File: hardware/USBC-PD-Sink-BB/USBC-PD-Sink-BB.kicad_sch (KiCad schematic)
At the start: 0 parts

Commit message: Started schematic.  Added docs for MCP22031 Sink Board
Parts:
- added J1: USB_C_Receptacle_USB2.0_16P, symbol Connector:USB_C_Receptacle_USB2.0_16P
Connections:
- new net: J1.A1 (GND), J1.A12 (GND), J1.B1 (GND), J1.B12 (GND)
- new net: J1.A4 (VBUS), J1.A9 (VBUS), J1.B4 (VBUS), J1.B9 (VBUS)
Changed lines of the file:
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@@
 		(title "USB C PD Sink Breakout Board")
+	)
+	(symbol
+		(lib_id "Connector:USB_C_Receptacle_USB2.0_16P")
+		(at 31.75 86.36 0)
+		(unit 1)
+		(exclude_from_sim no)
+		(in_bom yes)
+		(on_board yes)
+		(dnp no)
+		(fields_autoplaced yes)
+		(property "Reference" "J1"
+			(at 31.75 63.5 0)
+			(effects
+				(font
+					(size 1.27 1.27)
+				)
+			)
+		)
+		(property "Value" "USB_C_Receptacle_USB2.0_16P"
+			(at 31.75 66.04 0)
+			(effects
+				(font
+					(size 1.27 1.27)
+				)
+			)
+		)
+		(property "Footprint" ""
+			(at 35.56 86.36 0)
+			(effects
+				(font
+					(size 1.27 1.27)
+				)
+				(hide yes)
+			)
+		)
+		(property "Datasheet" "https://www.usb.org/sites/default/files/documents/usb_type-c.zip"
+			(at 35.56 86.36 0)
+			(effects
+				(font
+					(size 1.27 1.27)
+				)
+				(hide yes)
+			)
+		)
+		(property "Description" "USB 2.0-only 16P Type-C Receptacle connector"
+			(at 31.75 86.36 0)
+			(effects
+				(font
+					(size 1.27 1.27)
+				)
+				(hide yes)
+			)
+		)
+		(pin "B6"
+		)
+		(pin "A6"
+		)
+		(pin "B8"
+		)
+		(pin "A8"
+		)
+		(pin "B4"
+		)
+		(pin "B7"
+		)
+		(pin "A12"
+		)
+		(pin "A5"
+		)
+		(pin "A1"
+		)
+		(pin "S1"
+		)
+		(pin "A4"
+		)
+		(pin "A9"
+		)
+		(pin "B9"
+		)
+		(pin "B12"
+		)
+		(pin "B1"
+		)
+		(pin "A7"
+		)
+		(pin "B5"
+		)
+		(instances
+			(project ""
+				(path "/244fbf81-301d-43a9-8691-1c7dc9ccb063"
+					(reference "J1")
+					(unit 1)
+				)
+			)
+		)
 	)
 	(sheet_instances

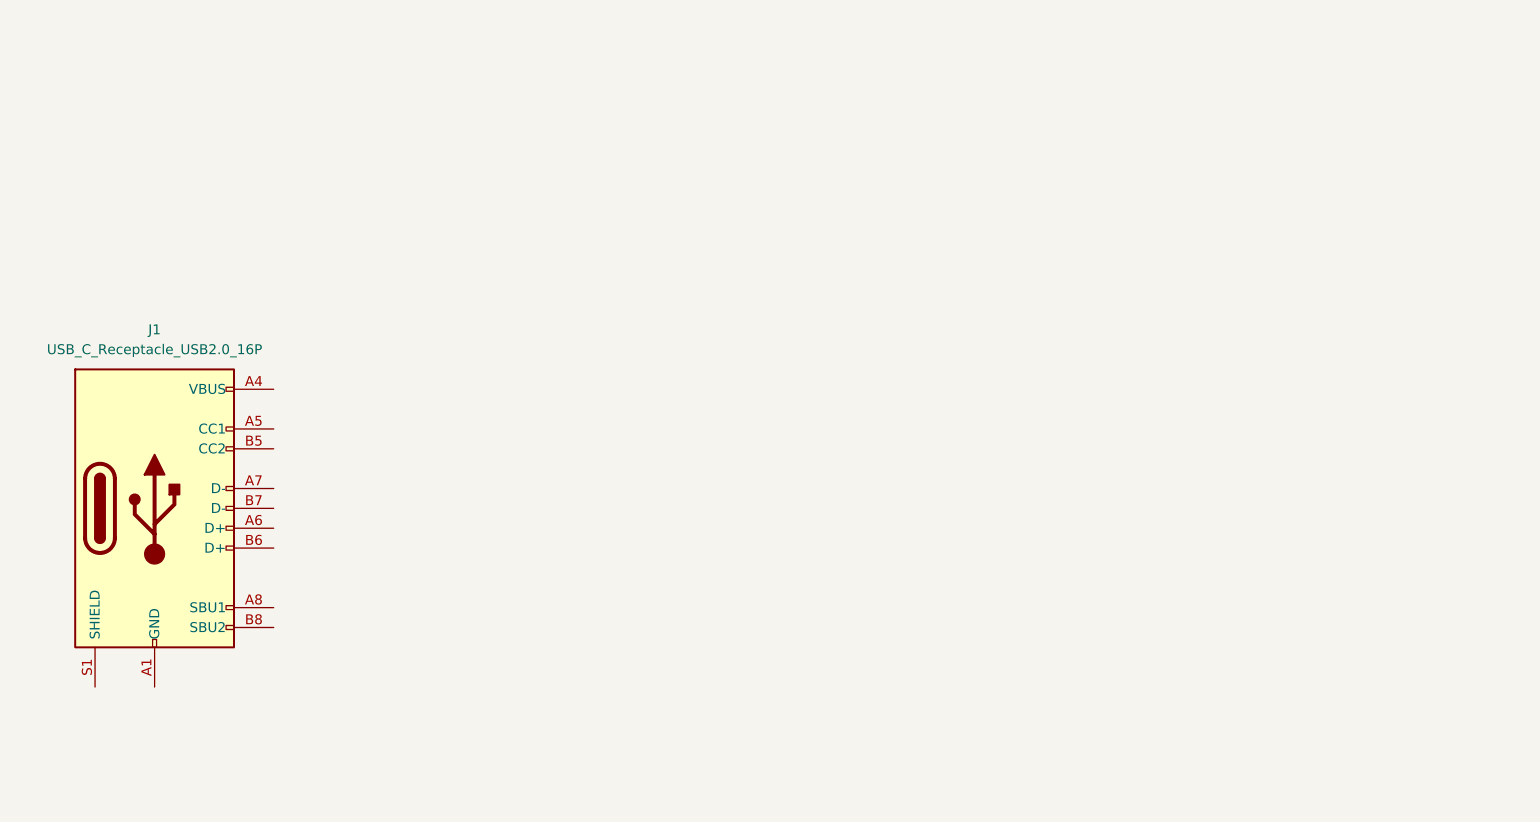
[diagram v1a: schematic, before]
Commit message: Updated schematic.  Added MCP22301
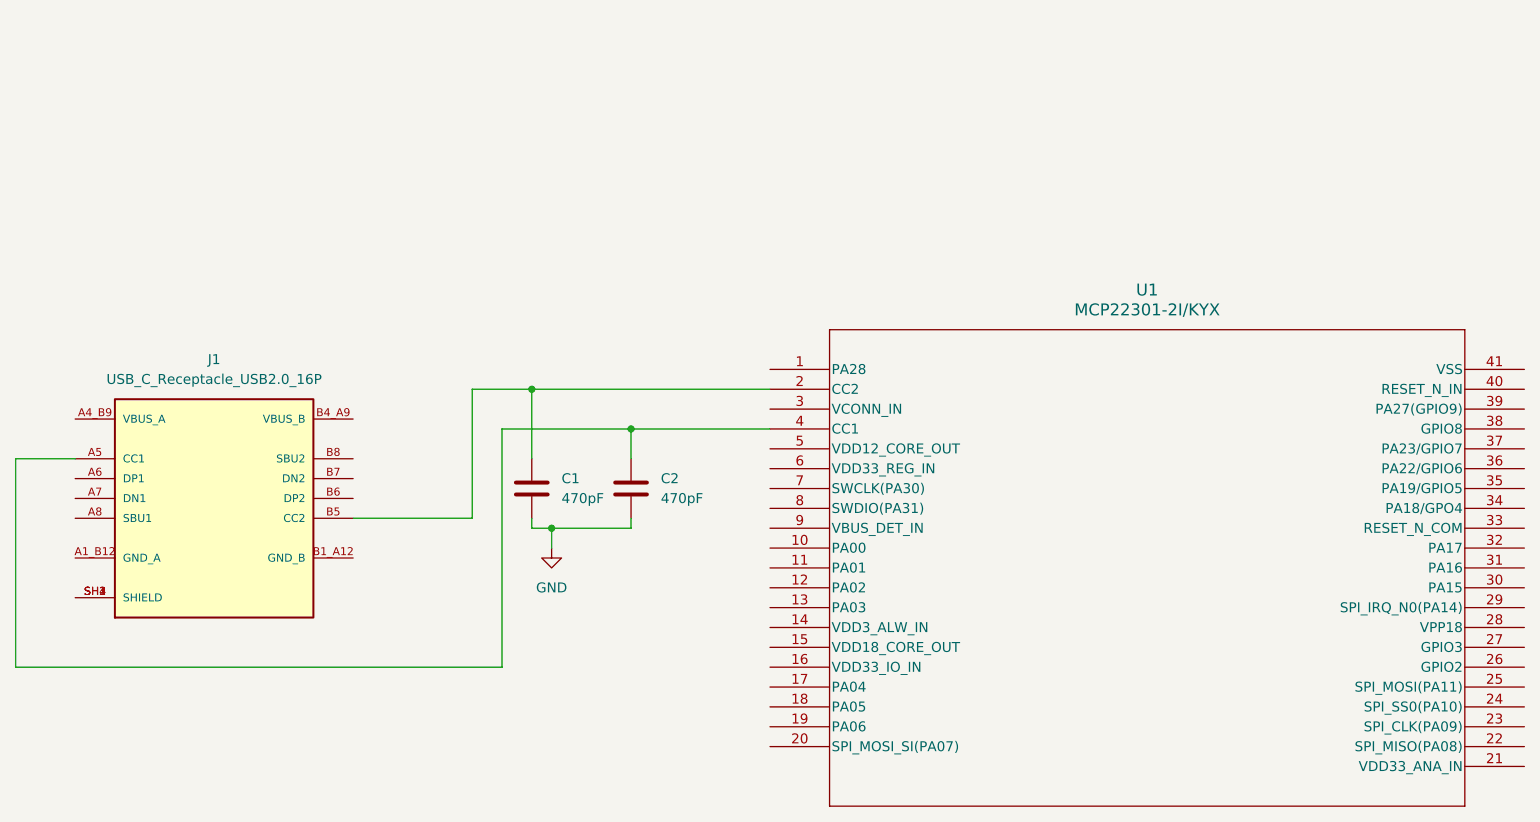
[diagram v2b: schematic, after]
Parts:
- added C1, C2: 470pF, symbol Device:C
- added U1: MCP22301-2I/KYX, MCP22301:VQFN40_KYX_MCH, symbol MCP22301:MCP22301-2I_KYX
- J1: footprint (none) -> USB4215-03-A_REVA:GCT_USB4215-03-A_REVA; symbol Connector:USB_C_Receptacle_USB2.0_16P -> USB421503:USB4215-03-A_REVA; CREATOR (none) -> Amina; Check_prices (none) -> https://www.snapeda.com/parts/USB4215-03-A/Global+Connector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; Description_1 (none) -> USB-C (USB TYPE-C) USB 2.0 Receptacle Connector 24 (16+8 Du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; DigiKey_Part_Number (none) -> 2073-USB4215-03-ATR-ND; MANUFACTURER (none) -> Global Connector Technology; MAXIMUM_PACKAGE_HEIGHT (none) -> 3.16mm; MF (none) -> Global Connector Technology; MP (none) -> USB4215-03-A; PARTREV (none) -> A; Package (none) -> None; STANDARD (none) -> Manufacturer Recommendations; SnapEDA_Link (none) -> https://www.snapeda.com/parts/USB4215-03-A/Global+Connector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; VERIFIER (none) -> Your name, use the same always
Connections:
- net at J1.A5 (CC1): now also C2.1, U1.4 (CC1)
- net at J1.B5 (CC2): now also C1.1, U1.2 (CC2)
- new net: J1.SH1 (SHIELD), J1.SH2 (SHIELD), J1.SH3 (SHIELD), J1.SH4 (SHIELD)
- new net GND: C1.2, C2.2

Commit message: Updated USB-C connector and MCP22301 symbols. Updated schematic with revised symbols
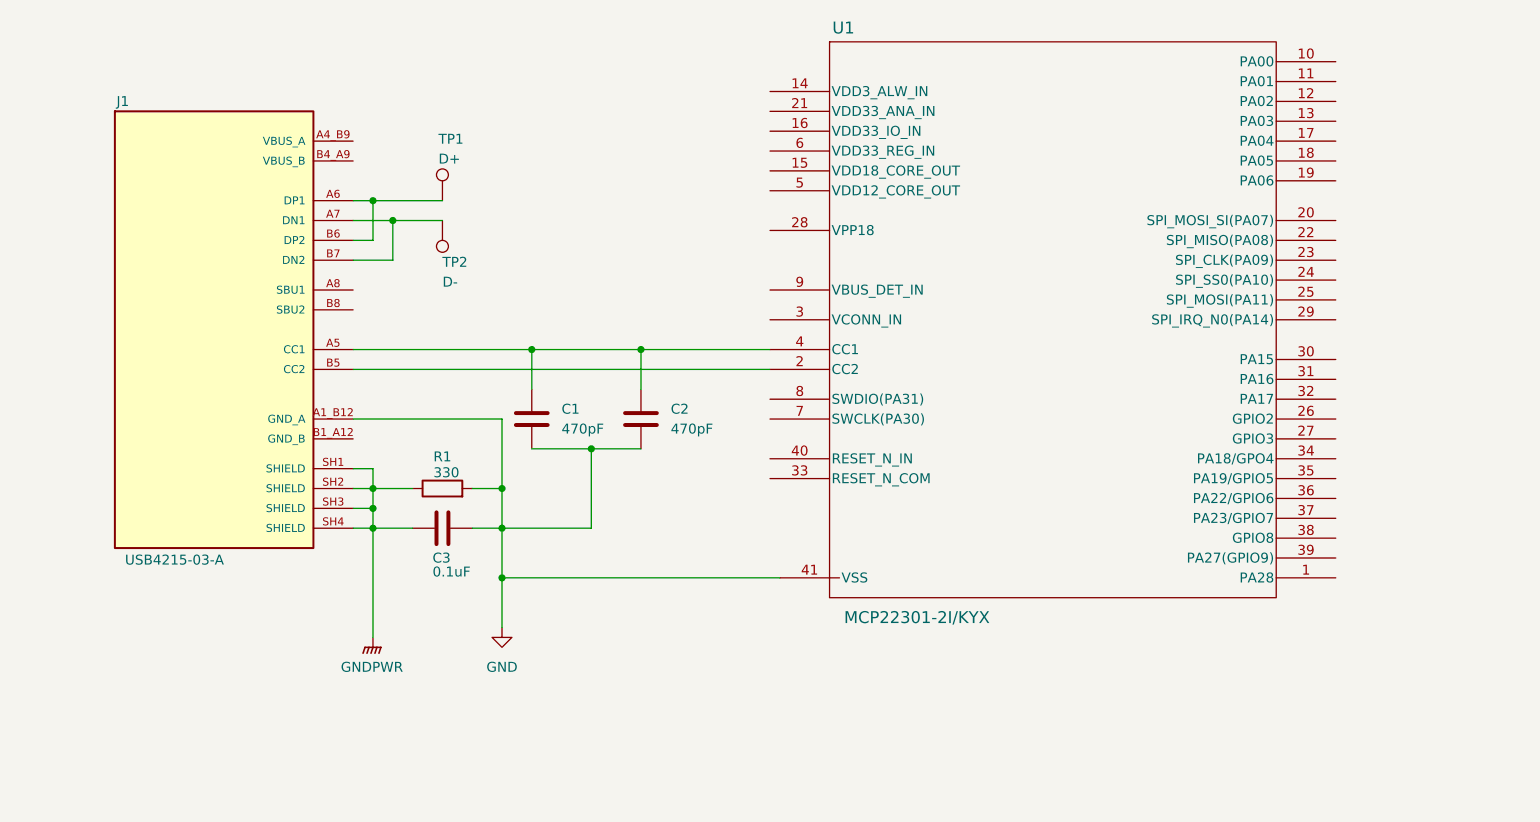
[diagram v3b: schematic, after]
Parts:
- added C3: 0.1uF, symbol Device:C
- added R1: 330, symbol Device:R
- added TP1: D+, symbol Connector:TestPoint
- added TP2: D-, symbol Connector:TestPoint
- J1: value USB_C_Receptacle_USB2.0_16P -> USB4215-03-A
- U1: footprint MCP22301:VQFN40_KYX_MCH -> VQFN40_KYX_MCH
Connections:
- net GND: now also J1.A1_B12 (GND_A), U1.41 (VSS), C3.1, R1.2
- net at C2.1, J1.A5 (CC1), U1.4 (CC1): now also C1.1
- net at J1.A6 (DP1): now also J1.B6 (DP2), TP1.1
- net at J1.A7 (DN1): now also J1.B7 (DN2), TP2.1
- net at J1.B5 (CC2), U1.2 (CC2): no longer C1.1
- net GNDPWR: now reaches J1.SH1 (SHIELD), J1.SH2 (SHIELD), J1.SH3 (SHIELD), J1.SH4 (SHIELD)
- net GNDPWR: now also C3.2, R1.1
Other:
- moved on the sheet: C1, C2
